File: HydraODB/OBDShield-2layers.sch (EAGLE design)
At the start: 24 parts, among them IC1 LM317MABDT, J1 HYDRABUS_SHIELD_CON_HEADER_2X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, J2 HYDRABUS_SHIELD_CON_HEADER_2X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, J3 HYDRABUS_SHIELD_CON_HEADER_2X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, U1 SN65HVD233DG4, U2 SN65HVD233DG4

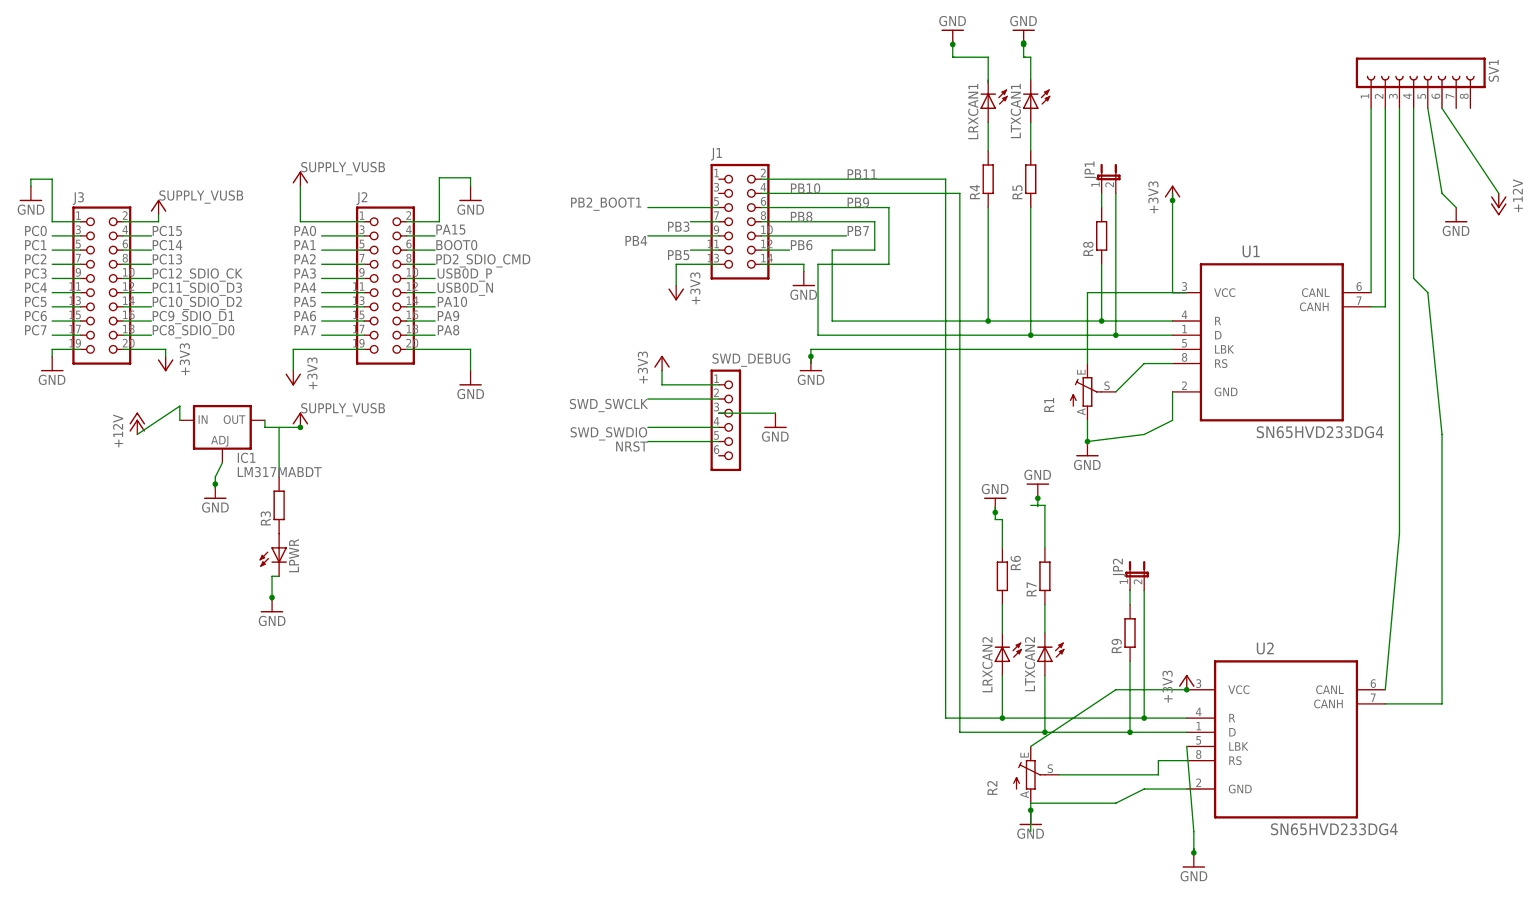
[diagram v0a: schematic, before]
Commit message: Corrected J2 mirror
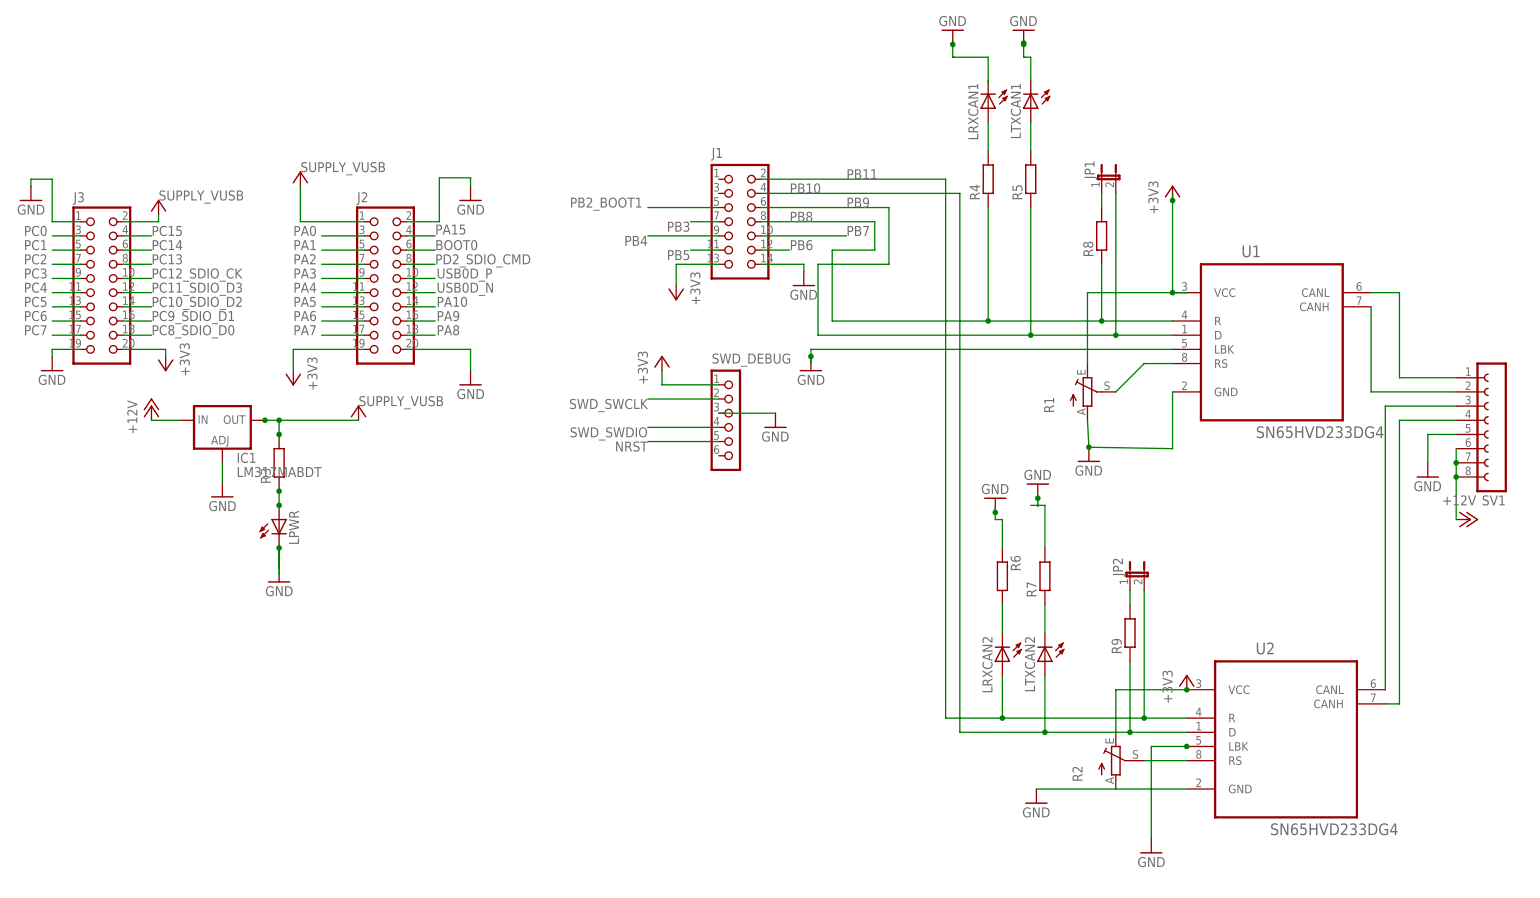
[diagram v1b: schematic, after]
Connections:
- net +12V: now also SV1.7, SV1.8
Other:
- moved on the sheet: LPWR, R2, R3, SV1
